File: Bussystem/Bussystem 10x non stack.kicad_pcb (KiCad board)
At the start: 2 copper layers, 176 x 63 mm, 13 parts, among them J1 PCIE-098-02-X-D-TH, J10 PCIE-098-02-X-D-TH, J2 PCIE-098-02-X-D-TH, J3 PCIE-098-02-X-D-TH, J4 PCIE-098-02-X-D-TH, J5 PCIE-098-02-X-D-TH, J6 PCIE-098-02-X-D-TH, J7 PCIE-098-02-X-D-TH, J8 PCIE-098-02-X-D-TH, J9 PCIE-098-02-X-D-TH

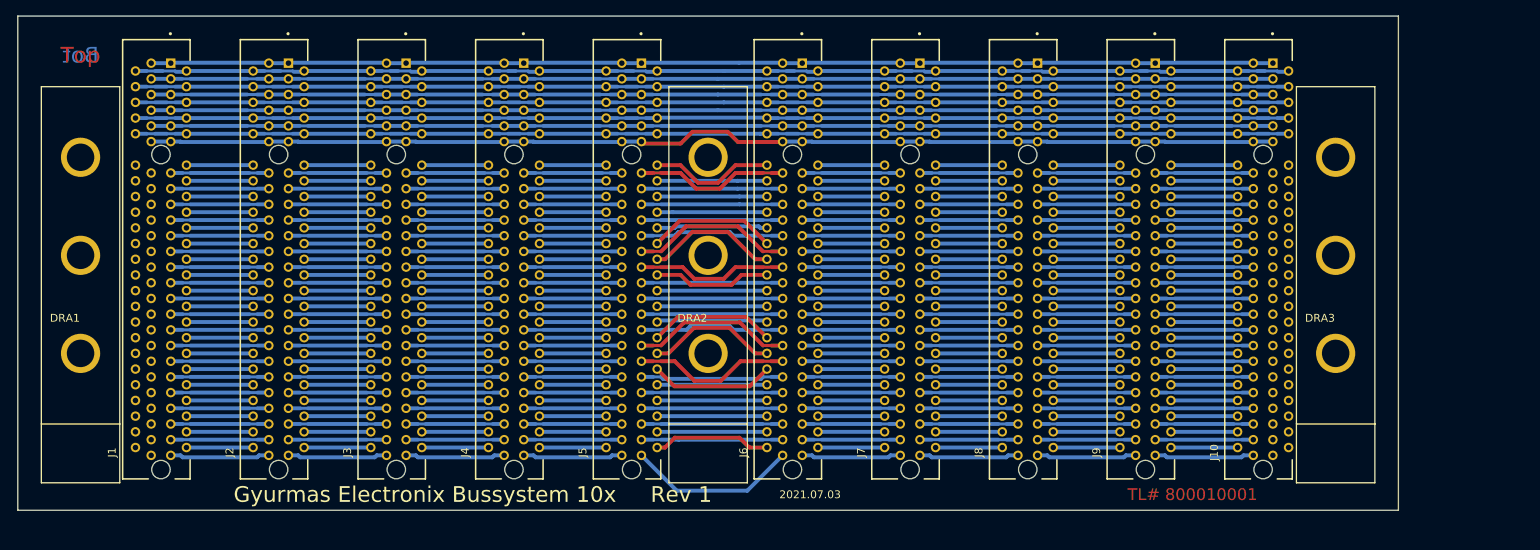
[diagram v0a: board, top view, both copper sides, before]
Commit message: Had to change pitch to 20mm because wago236-416 wouldnt fit.
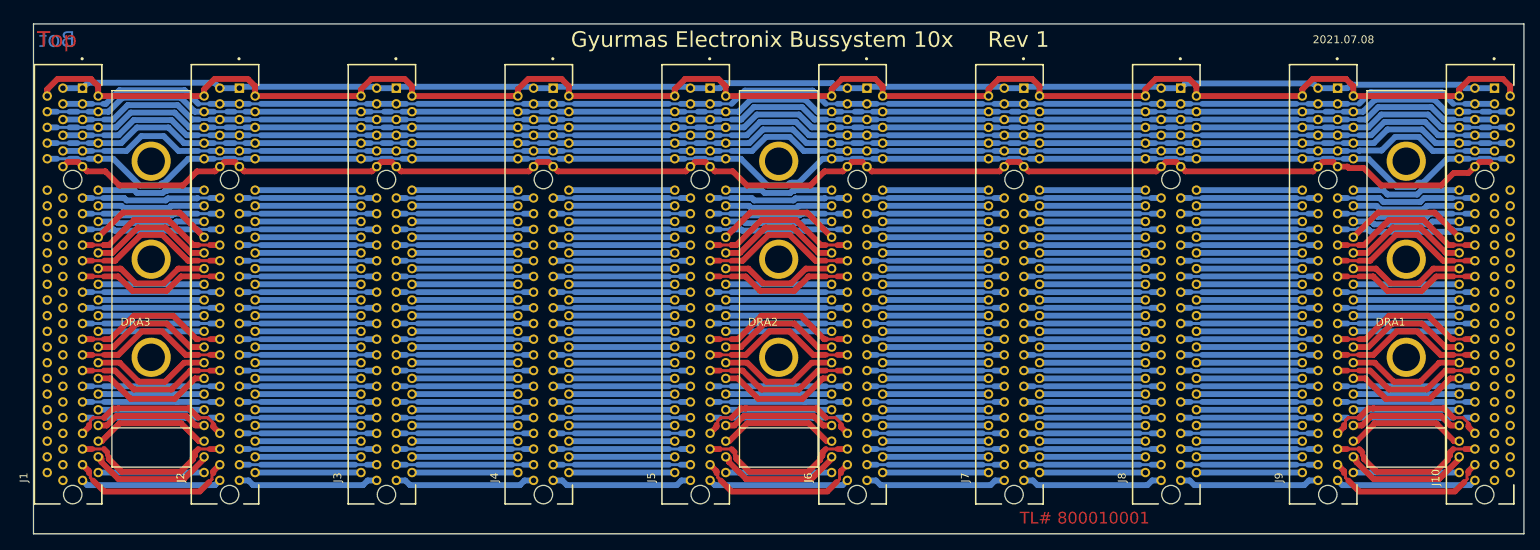
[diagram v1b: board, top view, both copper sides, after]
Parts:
- moved DRA1 169.0 mm to (215.0, 75.0)
- moved DRA3 151.0 mm to (55.0, 75.0)
- moved J10 28.4 mm to (224.4, 78.2)
- moved J9 23.5 mm to (204.4, 78.2)
- moved J8 18.5 mm to (184.4, 78.2)
- moved J7 13.6 mm to (164.4, 78.2)
- moved J1 11.7 mm to (44.4, 78.2)
- moved J5 9.31 mm to (124.4, 78.2)
- moved DRA2 9.01 mm to (135.0, 75.0)
- moved J6 8.85 mm to (144.4, 78.2)
- moved J2 7.02 mm to (64.4, 78.2)
- moved J4 4.92 mm to (104.4, 78.2)
- moved J3 3.43 mm to (84.4, 78.2)
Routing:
- net Net-(J1-PadA2): track 147.6 -> 216.8 mm
- net Net-(J1-PadA11): track 144.6 -> 197.8 mm
- net Net-(J1-PadA10): track 147.0 -> 195.1 mm
- net Net-(J1-PadA9): track 143.0 -> 187.0 mm
- net Net-(J1-PadA7): track 143.0 -> 186.9 mm
- net Net-(J1-PadA6): track 147.0 -> 190.8 mm
- net Net-(J1-PadA8): track 147.0 -> 190.7 mm
- net Net-(J1-PadA3): track 143.0 -> 186.7 mm
- net Net-(J1-PadA5): track 143.0 -> 186.7 mm
- net Net-(J1-PadA4): track 147.0 -> 190.5 mm
- net Net-(J1-PadA1): track 143.6 -> 185.5 mm
- net Net-(J1-PadA47): track 12.5 -> 21.7 mm
- net Net-(J10-PadB47): track 12.5 -> 21.7 mm
- net Net-(J1-PadA43): track 12.5 -> 21.3 mm
- net Net-(J10-PadB43): track 12.5 -> 21.3 mm
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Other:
- board size 176 x 63 mm -> 190 x 65 mm
- board text added: "2021.07.08"
- board text removed: "2021.07.03"

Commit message: new Teensy4 buscontroller added
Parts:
- added G***: Gyurmas Electronix, Gyurmas:GyLogo2_1, F.Cu at (114.5, 96.0)
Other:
- board text added: "Designed by Martin Gyurkó"
- board text added: "JLCJLCJLCJLC"
- board text added: "Universal Bussystem 10x Rev 1"
- board text removed: "Gyurmas Electronix Bussystem 10x Rev 1"

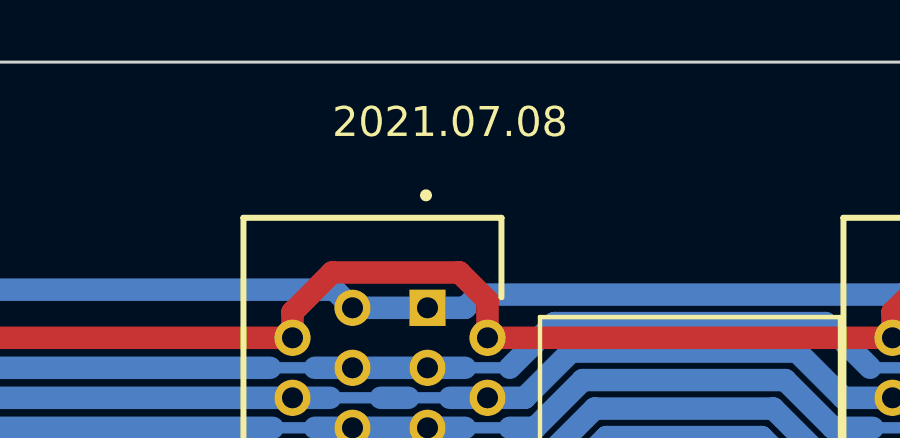
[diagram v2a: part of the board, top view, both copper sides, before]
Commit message: some new parts in the Buscontroller T1
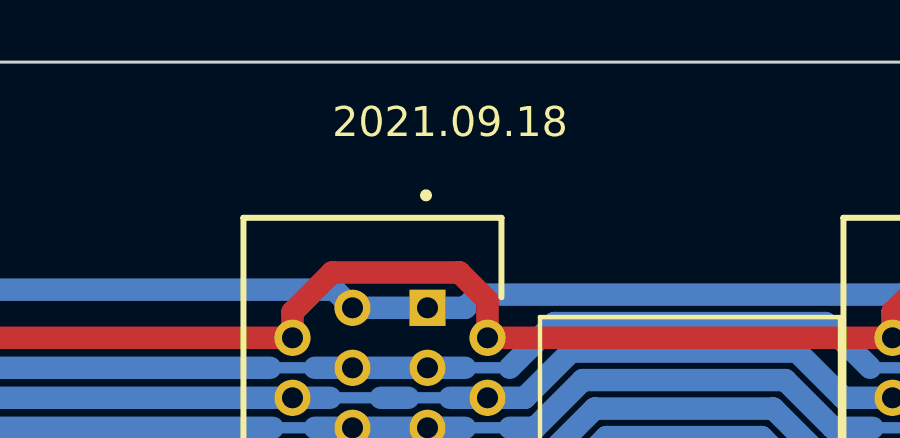
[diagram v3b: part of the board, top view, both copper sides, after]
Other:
- board text added: "2021.09.18"
- board text removed: "2021.07.08"
